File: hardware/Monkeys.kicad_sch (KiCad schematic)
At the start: 156 parts, among them IC1 SI4702-C19-GM, J1 JTAG, J2 3.3vSerial, J3 Therm, J4 PJ-320D-4A, J5 10118194-0001LF, Q1 BSS138, Q2 SI2302, Q3 MMBT3904, Q4 MMBT3904, Q5 MMBT3904, Q6 MMBT3904, SW1 SW_Push, SW2 SW_Push, SW3 SW_Push, SW4 SW_Push, SW5 SPDT_Switch, SW6 SW_MEC_5E, SW7 SPDT_Switch, U1 BQ24072RGT, U2 RT9080-33GJ5, U3 CH340C, U4 LM4808, U5 InfraredReceiver, U6 ESP32-WROOM-32E(8MB), U7 Boost5V, U8 MAX9814, Y1 32.768KHZ, Y2 32.768KHZ

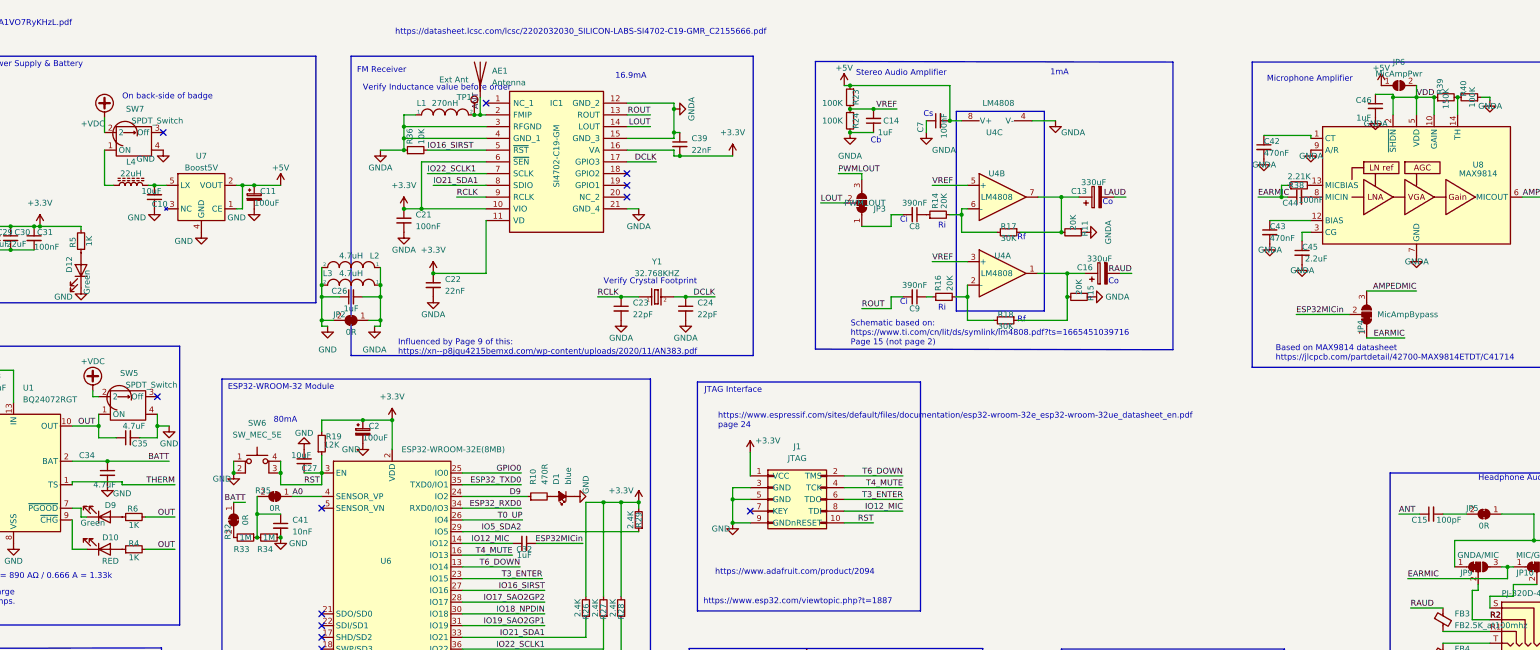
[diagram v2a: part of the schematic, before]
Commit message: hardware: Badge revision 3.6
In this revision changes were made to the following components:

- Change C42 in stereo amplifier from 390nF to 470nF
- Changed JP4 default state (Microphone amplifier - enable amplifier)

This spin of the hardware went to initial manufacturing with the gerbers
provided on September 9th, 2023.
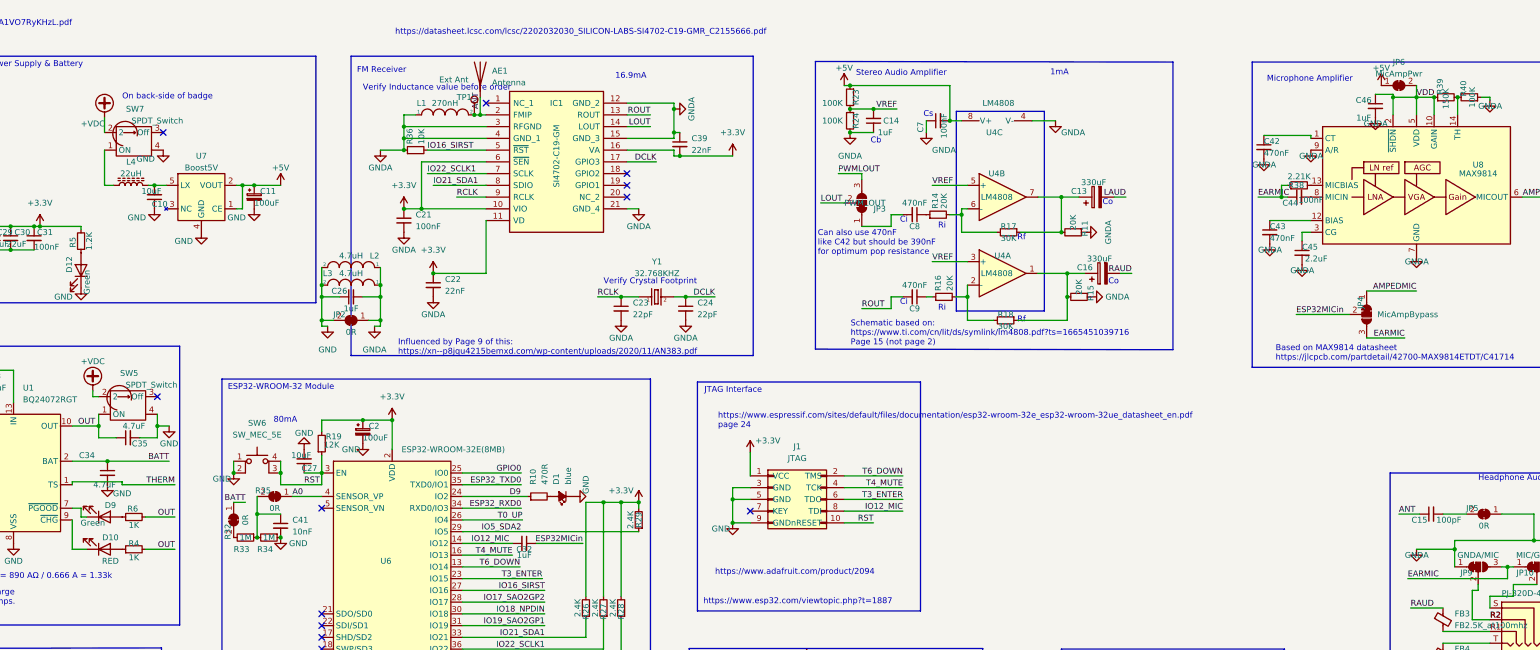
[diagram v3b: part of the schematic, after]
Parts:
- C8, C9: value 390nF -> 470nF; footprint monkeys20221112:C_0805_2012Metric -> monkeys20221112:C_0402_1005Metric; JLCPCB Part #（optional) C327132 -> C147712; Manufacturer_Part_Number CC0805KKX7R7BB394 -> C1005X5R474KDTS
- D10: JLCPCB Part #（optional) C72044 -> C2286; Manufacturer_Part_Number 19-217/R6C-AL1M2VY/3T -> KT-0603R
- JP6: footprint Jumper:SolderJumper-2_P1.3mm_Open_RoundedPad1.0x1.5mm -> Jumper:SolderJumper-2_P1.3mm_Bridged_RoundedPad1.0x1.5mm; symbol Jumper:SolderJumper_2_Open -> Jumper:SolderJumper_2_Bridged
- R5: value 1K -> 1.2K; JLCPCB Part #（optional) C100046 -> C724883; Manufacturer_Part_Number RC0805JR-071KL -> AR05FTDW1201; SeeedSKU 301010311 -> (none)
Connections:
- net AMPEDMIC: now also JP4.1 (A); no longer JP4.3 (B)
- net EARMIC: now also JP4.3 (B); no longer JP4.1 (A)
- net GNDA: now also JP10.3 (B), JP5.1 (A), JP9.1 (A)
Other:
- note added: "Can also use 470nF like C42 but should be 390nF for optimum pop resistance"

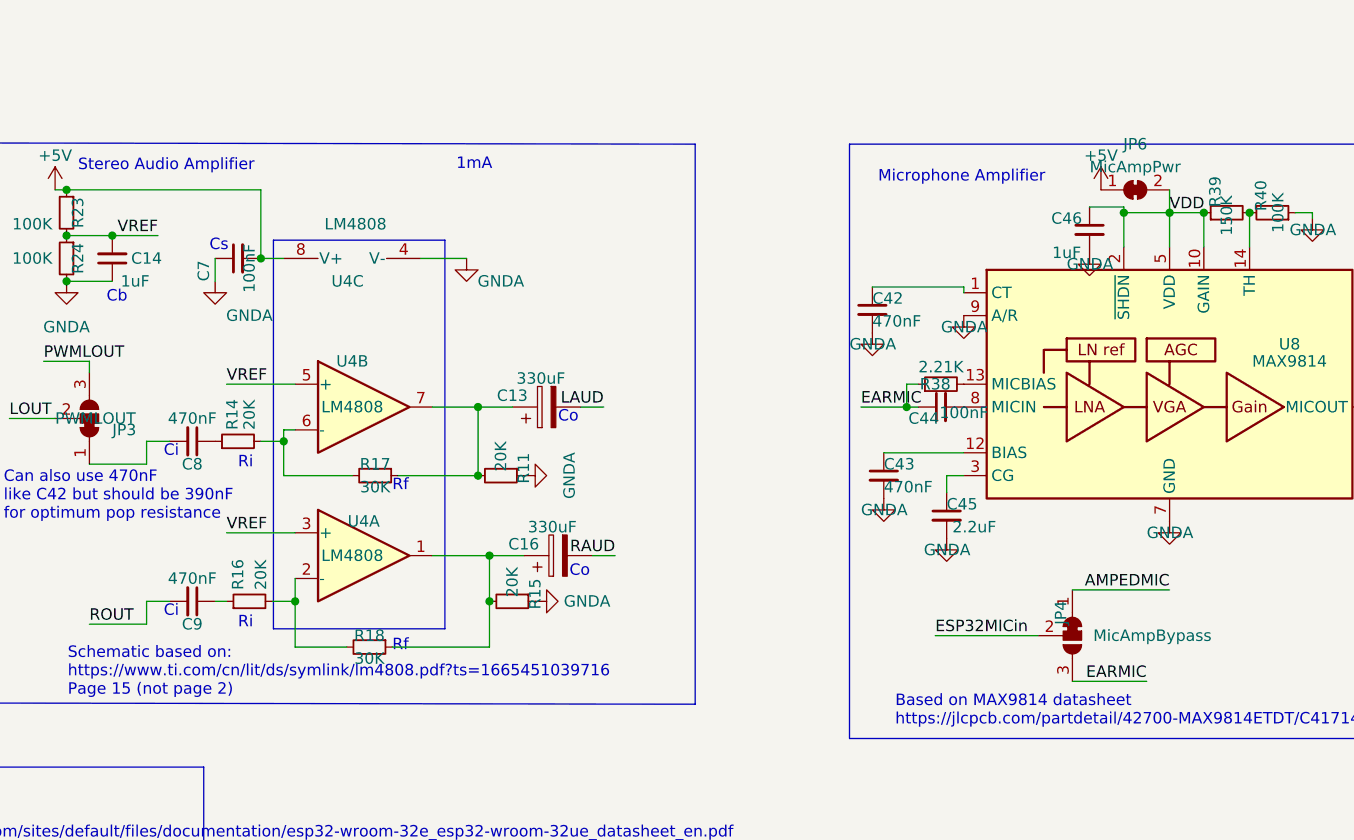
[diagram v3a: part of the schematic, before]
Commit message: hardware: Badge revision 3.7
In this revision changes were made to the following components:

- Change C42 in stereo amplifier from 470nF to 390nF
- Changed JP4 default state (Microphone amplifier - disabled amp by
  default)

This spin of the hardware went to initial manufacturing with the gerbers
provided on September 15th, 2023.
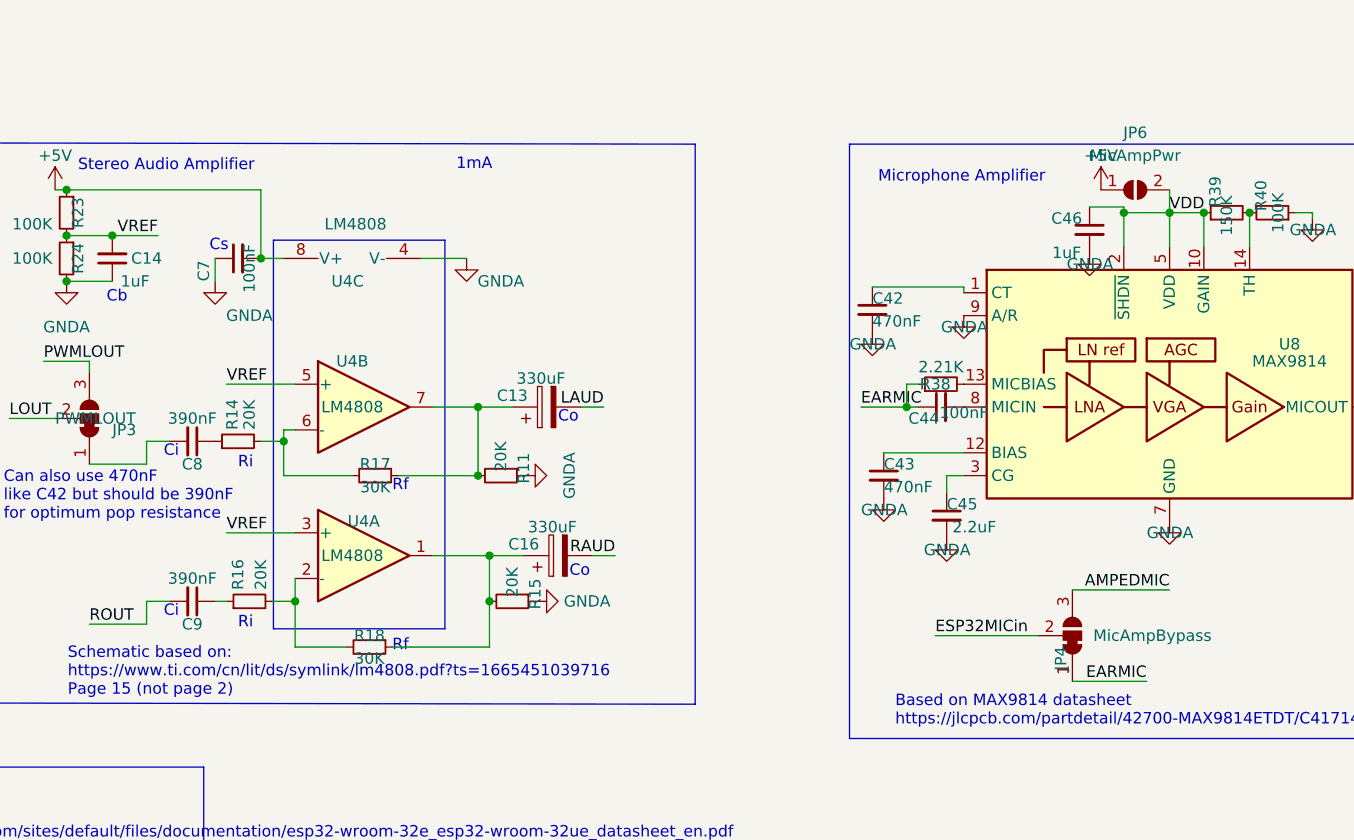
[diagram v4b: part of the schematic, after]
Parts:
- C10, C27: JLCPCB Part #（optional) C326057 -> C19702; Manufacturer_Part_Number CC0603KRX5R6BB106 -> CL10A106KP8NNNC
- C29, C30: JLCPCB Part #（optional) C2835558 -> C45783; Manufacturer_Part_Number C0805X6S226M6R3NT -> CL21A226MAQNNNE
- C8, C9: value 470nF -> 390nF; JLCPCB Part #（optional) C147712 -> C350937; Manufacturer_Part_Number C1005X5R474KDTS -> GRM155R61A394KE15D
- JP6: footprint Jumper:SolderJumper-2_P1.3mm_Bridged_RoundedPad1.0x1.5mm -> Jumper:SolderJumper-2_P1.3mm_Open_RoundedPad1.0x1.5mm; symbol Jumper:SolderJumper_2_Bridged -> Jumper:SolderJumper_2_Open
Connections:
- net AMPEDMIC: now also JP4.3 (B); no longer JP4.1 (A)
- net EARMIC: now also JP4.1 (A); no longer JP4.3 (B)
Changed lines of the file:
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@@
       )
     )
+    (symbol "Jumper:SolderJumper_2_Open" (pin_names (offset 0) hide) (in_bom yes) (on_board yes)
+      (property "Reference" "JP" (id 0) (at 0 2.032 0)
+        (effects (font (size 1.27 1.27)))
+      )
+      (property "Value" "SolderJumper_2_Open" (id 1) (at 0 -2.54 0)
+        (effects (font (size 1.27 1.27)))
+      )
+      (property "Footprint" "" (id 2) (at 0 0 0)
+        (effects (font (size 1.27 1.27)) hide)
+      )
+      (property "Datasheet" "~" (id 3) (at 0 0 0)
+        (effects (font (size 1.27 1.27)) hide)
+      )
+      (property "ki_keywords" "solder jumper SPST" (id 4) (at 0 0 0)
+        (effects (font (size 1.27 1.27)) hide)
+      )
+      (property "ki_description" "Solder Jumper, 2-pole, open" (id 5) (at 0 0 0)
+        (effects (font (size 1.27 1.27)) hide)
+      )
+      (property "ki_fp_filters" "SolderJumper*Open*" (id 6) (at 0 0 0)
+        (effects (font (size 1.27 1.27)) hide)
+      )
+      (symbol "SolderJumper_2_Open_0_1"
+        (arc (start -0.254 1.016) (mid -1.27 0) (end -0.254 -1.016)
+          (stroke (width 0) (type default) (color 0 0 0 0))
+          (fill (type none))
+        )
+        (arc (start -0.254 1.016) (mid -1.27 0) (end -0.254 -1.016)
+          (stroke (width 0) (type default) (color 0 0 0 0))
+          (fill (type outline))
+        )
+        (polyline
+          (pts
+            (xy -0.254 1.016)
+            (xy -0.254 -1.016)
+          )
+          (stroke (width 0) (type default) (color 0 0 0 0))
+          (fill (type none))
+        )
+        (polyline
+          (pts
+            (xy 0.254 1.016)
+            (xy 0.254 -1.016)
+          )
+          (stroke (width 0) (type default) (color 0 0 0 0))
+          (fill (type none))
+        )
+        (arc (start 0.254 -1.016) (mid 1.27 0) (end 0.254 1.016)
+          (stroke (width 0) (type default) (color 0 0 0 0))
+          (fill (type none))
+        )
+        (arc (start 0.254 -1.016) (mid 1.27 0) (end 0.254 1.016)
+          (stroke (width 0) (type default) (color 0 0 0 0))
+          (fill (type outline))
+        )
+      )
+      (symbol "SolderJumper_2_Open_1_1"
+        (pin passive line (at -3.81 0 0) (length 2.54)
+          (name "A" (effects (font (size 1.27 1.27))))
+          (number "1" (effects (font (size 1.27 1.27))))
+        )
+        (pin passive line (at 3.81 0 180) (length 2.54)
+          (name "B" (effects (font (size 1.27 1.27))))
+          (number "2" (effects (font (size 1.27 1.27))))
+        )
+      )
+    )
     (symbol "Jumper:SolderJumper_3_Bridged12" (pin_names (offset 0) hide) (in_bom yes) (on_board yes)
       (property "Reference" "JP" (id 0) (at -2.54 -2.54 0)
@@
     (in_bom yes) (on_board yes)
     (property "Reference" "C8" (id 0) (at 251.46 50.8 90))
-    (property "Value" "470nF" (id 1) (at 251.46 45.72 90))
+    (property "Value" "390nF" (id 1) (at 251.46 45.72 90))
     (property "Footprint" "monkeys20221112:C_0402_1005Metric" (id 2) (at 251.46 48.26 0)
       (effects (font (size 1.27 1.27)) hide)
@@
       (effects (font (size 1.27 1.27)) hide)
     )
-    (property "Manufacturer_Part_Number" "C1005X5R474KDTS" (id 5) (at 251.46 48.26 0)
+    (property "Manufacturer_Part_Number" "GRM155R61A394KE15D" (id 5) (at 251.46 48.26 0)
       (effects (font (size 1.27 1.27)) hide)
     )
@@
       (effects (font (size 1.27 1.27)) hide)
     )
-    (property "JLCPCB Part #（optional)" "C147712" (id 8) (at 251.46 48.26 0)
+    (property "JLCPCB Part #（optional)" "C350937" (id 8) (at 251.46 48.26 0)
       (effects (font (size 1.27 1.27)) hide)
     )
@@
     (pin "2")
   )
-  (symbol (lib_id "Jumper:SolderJumper_2_Bridged") (at 356.235 20.32 0) (unit 1)
+  (symbol (lib_id "Jumper:SolderJumper_2_Open") (at 356.235 20.32 0) (unit 1)
     (in_bom yes) (on_board yes) (fields_autoplaced)
-    (property "Reference" "JP6" (id 0) (at 356.235 15.24 0))
-    (property "Value" "MicAmpPwr" (id 1) (at 356.235 17.78 0))
-    (property "Footprint" "Jumper:SolderJumper-2_P1.3mm_Bridged_RoundedPad1.0x1.5mm" (id 2) (at 356.235 20.32 0)
+    (property "Reference" "JP6" (id 0) (at 356.235 13.97 0))
+    (property "Value" "MicAmpPwr" (id 1) (at 356.235 16.51 0))
+    (property "Footprint" "Jumper:SolderJumper-2_P1.3mm_Open_RoundedPad1.0x1.5mm" (id 2) (at 356.235 20.32 0)
       (effects (font (size 1.27 1.27)) hide)
     )
@@
       (effects (font (size 1.27 1.27)) hide)
     )
-    (property "Manufacturer_Part_Number" "C0805X6S226M6R3NT" (id 5) (at 52.07 53.34 0)
+    (property "Manufacturer_Part_Number" "CL21A226MAQNNNE" (id 5) (at 52.07 53.34 0)
       (effects (font (size 1.27 1.27)) hide)
     )
@@
       (effects (font (size 1.27 1.27)) hide)
     )
-    (property "JLCPCB Part #（optional)" "C2835558" (id 8) (at 52.07 53.34 0)
+    (property "JLCPCB Part #（optional)" "C45783" (id 8) (at 52.07 53.34 0)
       (effects (font (size 1.27 1.27)) hide)
     )
@@
     (pin "1")
   )
-  (symbol (lib_id "Jumper:SolderJumper_3_Bridged12") (at 349.25 69.85 270) (unit 1)
+  (symbol (lib_id "Jumper:SolderJumper_3_Bridged12") (at 349.25 69.85 270) (mirror x) (unit 1)
     (in_bom yes) (on_board yes)
-    (property "Reference" "JP4" (id 0) (at 347.98 67.31 0))
+    (property "Reference" "JP4" (id 0) (at 347.98 72.39 0))
     (property "Value" "MicAmpBypass" (id 1) (at 358.14 69.85 90))
     (property "Footprint" "monkeys20221112:SolderJumper-3_P1.3mm_Bridged12_RoundedPad1.0x1.5mm" (id 2) (at 349.25 69.85 0)
@@
     (in_bom yes) (on_board yes)
     (property "Reference" "C9" (id 0) (at 251.46 68.58 90))
-    (property "Value" "470nF" (id 1) (at 251.46 63.5 90))
+    (property "Value" "390nF" (id 1) (at 251.46 63.5 90))
     (property "Footprint" "monkeys20221112:C_0402_1005Metric" (id 2) (at 251.46 66.04 0)
       (effects (font (size 1.27 1.27)) hide)
@@
       (effects (font (size 1.27 1.27)) hide)
     )
-    (property "Manufacturer_Part_Number" "C1005X5R474KDTS" (id 5) (at 251.46 66.04 0)
+    (property "Manufacturer_Part_Number" "GRM155R61A394KE15D" (id 5) (at 251.46 66.04 0)
       (effects (font (size 1.27 1.27)) hide)
     )
@@
       (effects (font (size 1.27 1.27)) hide)
     )
-    (property "JLCPCB Part #（optional)" "C147712" (id 8) (at 251.46 66.04 0)
+    (property "JLCPCB Part #（optional)" "C350937" (id 8) (at 251.46 66.04 0)
       (effects (font (size 1.27 1.27)) hide)
     )
@@
       (effects (font (size 1.27 1.27)) hide)
     )
-    (property "Manufacturer_Part_Number" "C0805X6S226M6R3NT" (id 5) (at 55.88 53.34 0)
+    (property "Manufacturer_Part_Number" "CL21A226MAQNNNE" (id 5) (at 55.88 53.34 0)
       (effects (font (size 1.27 1.27)) hide)
     )
@@
       (effects (font (size 1.27 1.27)) hide)
     )
-    (property "JLCPCB Part #（optional)" "C2835558" (id 8) (at 55.88 53.34 0)
+    (property "JLCPCB Part #（optional)" "C45783" (id 8) (at 55.88 53.34 0)
       (effects (font (size 1.27 1.27)) hide)
     )
@@
       (effects (font (size 1.27 1.27)) hide)
     )
-    (property "Manufacturer_Part_Number" "CC0603KRX5R6BB106" (id 5) (at 86.995 44.45 0)
+    (property "Manufacturer_Part_Number" "CL10A106KP8NNNC" (id 5) (at 86.995 44.45 0)
       (effects (font (size 1.27 1.27)) hide)
     )
@@
       (effects (font (size 1.27 1.27)) hide)
     )
-    (property "JLCPCB Part #（optional)" "C326057" (id 8) (at 86.995 44.45 0)
+    (property "JLCPCB Part #（optional)" "C19702" (id 8) (at 86.995 44.45 0)
       (effects (font (size 1.27 1.27)) hide)
     )
@@
       (effects (font (size 1.27 1.27)) hide)
     )
-    (property "Manufacturer_Part_Number" "CC0603KRX5R6BB106" (id 5) (at 119.38 101.6 0)
+    (property "Manufacturer_Part_Number" "CL10A106KP8NNNC" (id 5) (at 119.38 101.6 0)
       (effects (font (size 1.27 1.27)) hide)
     )
@@
       (effects (font (size 1.27 1.27)) hide)
     )
-    (property "JLCPCB Part #（optional)" "C326057" (id 8) (at 119.38 101.6 0)
+    (property "JLCPCB Part #（optional)" "C19702" (id 8) (at 119.38 101.6 0)
       (effects (font (size 1.27 1.27)) hide)
     )
@@
     )
     (path "/1c3825db-66d0-4dc3-908e-2bc6cab09772"
-      (reference "C8") (unit 1) (value "470nF") (footprint "monkeys20221112:C_0402_1005Metric")
+      (reference "C8") (unit 1) (value "390nF") (footprint "monkeys20221112:C_0402_1005Metric")
     )
     (path "/959f42c5-4f62-4e6f-942b-f9c256b12a6d"
-      (reference "C9") (unit 1) (value "470nF") (footprint "monkeys20221112:C_0402_1005Metric")
+      (reference "C9") (unit 1) (value "390nF") (footprint "monkeys20221112:C_0402_1005Metric")
     )
     (path "/b5333a33-4d83-401d-96c3-ad9d8b26e4cb"
@@
     )
     (path "/282798a5-fbab-48e9-b569-1b1599aa22c9"
-      (reference "JP6") (unit 1) (value "MicAmpPwr") (footprint "Jumper:SolderJumper-2_P1.3mm_Bridged_RoundedPad1.0x1.5mm")
+      (reference "JP6") (unit 1) (value "MicAmpPwr") (footprint "Jumper:SolderJumper-2_P1.3mm_Open_RoundedPad1.0x1.5mm")
     )
     (path "/967568dd-2085-471e-9d69-3573289c64af"
